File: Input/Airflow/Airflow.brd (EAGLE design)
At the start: 20 x 13 mm, 10 parts, among them Q1 MOSFET-NCHANNELBSS123LT1G

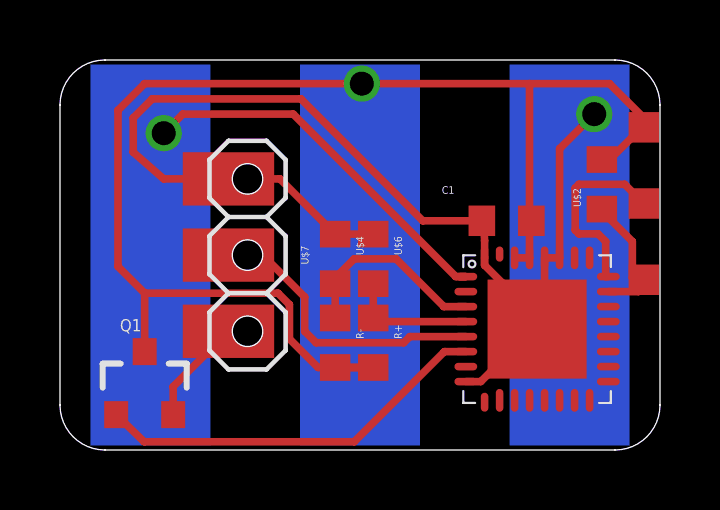
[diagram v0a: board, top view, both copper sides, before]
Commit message: Update Pinheader
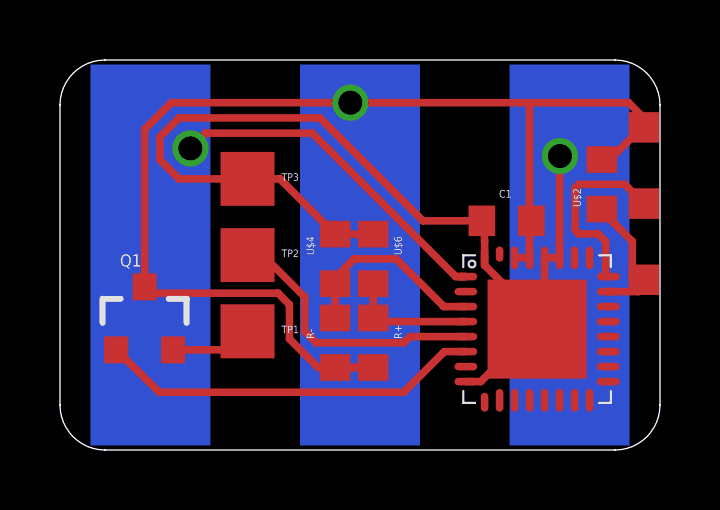
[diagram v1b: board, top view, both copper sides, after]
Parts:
- removed U$7: PINHD_32.54MOD, thar:PINHD_3_MOD
- added TP1, TP2, TP3: TPTP18SQ, testpad:TP18SQ
- moved Q1 2.16 mm to (4.57, 5.59)
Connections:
- net GND: now also TP3.TP; no longer U$7.P$1
- net N$6: now also TP2.TP; no longer U$7.P$2
- net N$7: now also TP1.TP; no longer U$7.P$3
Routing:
- net GND: track 54.6 -> 47.1 mm
- net VCC: track 53.1 -> 49.0 mm
- net N$12: track 16.9 -> 15.8 mm
- net N$7: track 3.54 -> 2.74 mm
- net N$6: track 9.88 -> 9.24 mm
